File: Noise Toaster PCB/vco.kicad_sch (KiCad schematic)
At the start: 18 parts, among them Q3 2N3904, Q4 2N3904, U1 LM324

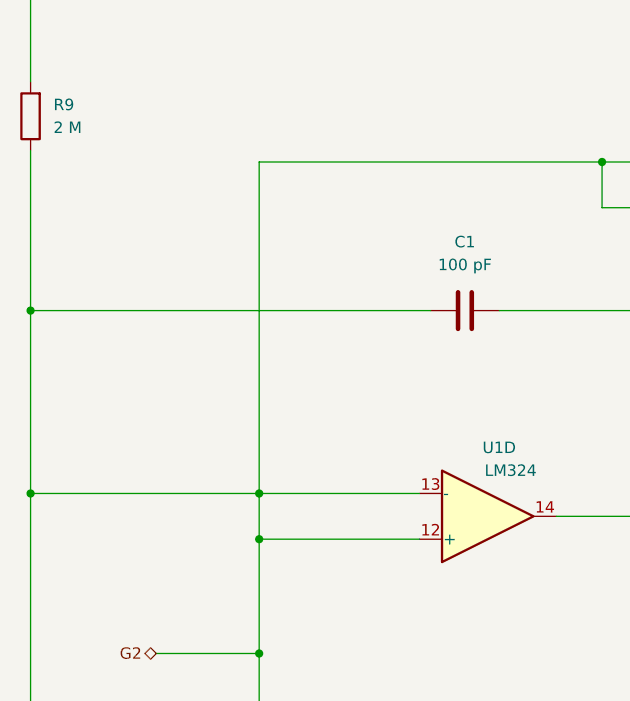
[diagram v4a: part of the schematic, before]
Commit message: placed pards of the pcb properly
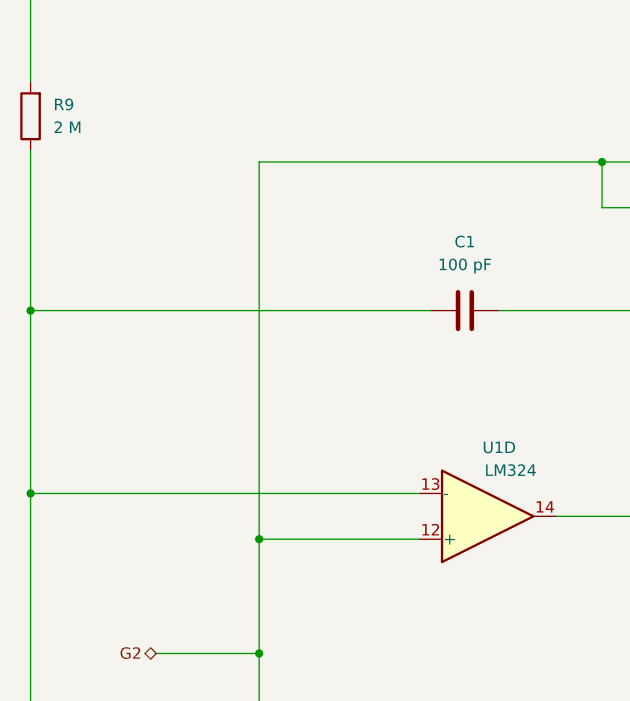
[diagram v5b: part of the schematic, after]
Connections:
- net G2: no longer C1.1, Q3.3 (C), R9.1, U1.13 (-)
- new net: C1.1, Q3.3 (C), R9.1, U1.13 (-)
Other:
- company: http://musicfromouterspace.com/analogsynth_new/NOISETOASTER/NOISETOASTER.php -> Music From Outer Space LLC
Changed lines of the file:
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@@
     (title "VCO - CV Mixer and Expo Converter")
     (rev "0.5")
-    (company "http://musicfromouterspace.com/analogsynth_new/NOISETOASTER/NOISETOASTER.php")
+    (company "Music From Outer Space LLC")
     (comment 1 "Licence: CC-BY-NC-SA")
     (comment 2 "Original Design by Ray Wilson")
-    (comment 3 "Music From Outer Space LLC")
+    (comment 3 "http://musicfromouterspace.com/analogsynth_new/NOISETOASTER/NOISETOASTER.php")
   )
   (junction (at 114.3 63.5) (diameter 0) (color 0 0 0 0)
@@
   (junction (at 88.9 110.49) (diameter 0) (color 0 0 0 0)
   )
-  (junction (at 50.8 147.32) (diameter 0) (color 0 0 0 0)
-  )
   (junction (at 25.4 147.32) (diameter 0) (color 0 0 0 0)
   )
@@
     (stroke (width 0) (type default))
   )
-  (wire (pts (xy 50.8 110.49) (xy 50.8 147.32))
+  (wire (pts (xy 50.8 110.49) (xy 50.8 152.4))
     (stroke (width 0) (type default))
   )
@@
     (stroke (width 0) (type default))
   )
-  (wire (pts (xy 50.8 152.4) (xy 50.8 147.32))
-    (stroke (width 0) (type default))
-  )
   (wire (pts (xy 88.9 110.49) (xy 88.9 115.57))
     (stroke (width 0) (type default))
@@
     (stroke (width 0) (type default))
   )
-  (wire (pts (xy 68.58 147.32) (xy 50.8 147.32))
-    (stroke (width 0) (type default))
-  )
   (wire (pts (xy 129.54 107.95) (xy 152.4 107.95))
     (stroke (width 0) (type default))
@@
     (stroke (width 0) (type default))
   )
-  (wire (pts (xy 50.8 147.32) (xy 25.4 147.32))
-    (stroke (width 0) (type default))
-  )
+  (wire (pts (xy 25.4 147.32) (xy 68.58 147.32))
+    (stroke (width 0) (type default))
+  )

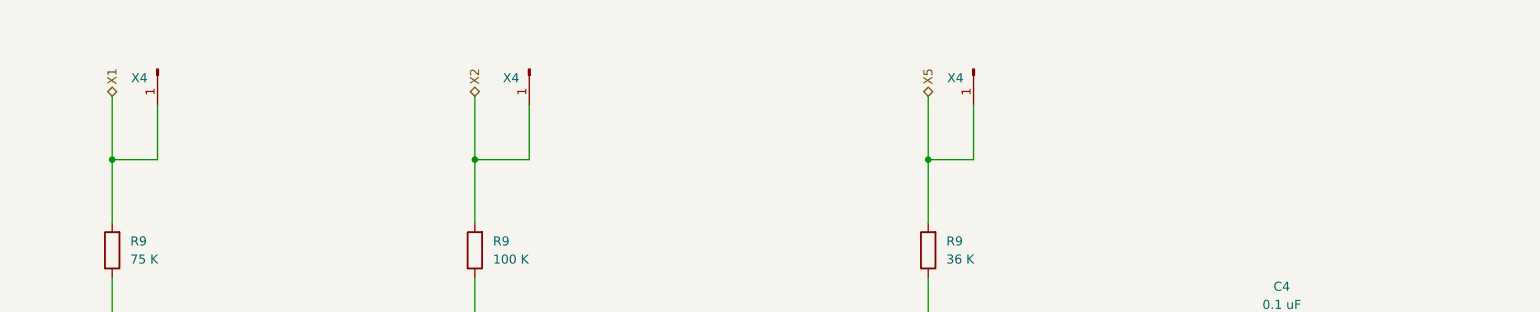
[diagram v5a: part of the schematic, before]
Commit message: changed header pins to groups
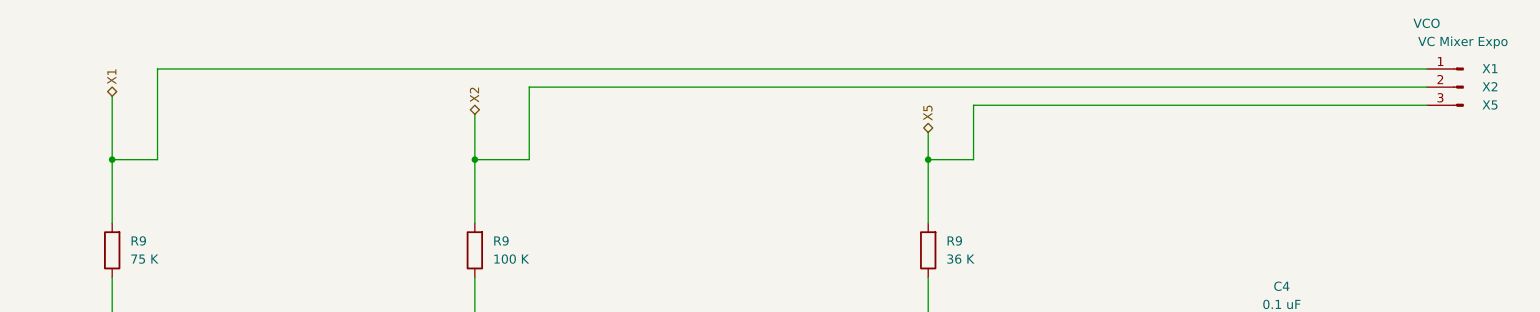
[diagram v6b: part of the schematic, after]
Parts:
- removed X4 (x3): ~, Connector_PinHeader_1.00mm:PinHeader_1x01_P1.00mm_Vertical, symbol Connector:Conn_01x01_Pin
- added J5: VCO, Connector_PinHeader_2.00mm:PinHeader_1x03_P2.00mm_Vertical, symbol Connector:Conn_01x03_Pin
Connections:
- net X1: now also J5.1 (Pin_1)
- net X2: now also J5.2 (Pin_2)
- net X5: now also J5.3 (Pin_3)
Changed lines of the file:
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@@
   (title_block
     (title "VCO - CV Mixer and Expo Converter")
-    (rev "0.5")
+    (rev "0.6")
     (company "Music From Outer Space LLC")
     (comment 1 "Licence: CC-BY-NC-SA")
@@
   (junction (at 101.6 127) (diameter 0) (color 0 0 0 0)
   )
+  (junction (at 114.3 83.82) (diameter 0) (color 0 0 0 0)
+  )
+  (junction (at 25.4 127) (diameter 0) (color 0 0 0 0)
+  )
   (junction (at 114.3 38.1) (diameter 0) (color 0 0 0 0)
   )
-  (junction (at 114.3 83.82) (diameter 0) (color 0 0 0 0)
-  )
-  (junction (at 25.4 127) (diameter 0) (color 0 0 0 0)
-  )
   (junction (at 25.4 83.82) (diameter 0) (color 0 0 0 0)
   )
   (junction (at 212.09 115.57) (diameter 0) (color 0 0 0 0)
   )
+  (junction (at 63.5 38.1) (diameter 0) (color 0 0 0 0)
+  )
   (junction (at 50.8 152.4) (diameter 0) (color 0 0 0 0)
   )
@@
   (junction (at 50.8 165.1) (diameter 0) (color 0 0 0 0)
   )
-  (junction (at 63.5 38.1) (diameter 0) (color 0 0 0 0)
-  )
   (junction (at 152.4 107.95) (diameter 0) (color 0 0 0 0)
   )
@@
     (stroke (width 0) (type default))
   )
+  (wire (pts (xy 247.65 25.4) (xy 69.85 25.4))
+    (stroke (width 0) (type default))
+  )
   (wire (pts (xy 114.3 38.1) (xy 121.92 38.1))
     (stroke (width 0) (type default))
@@
     (stroke (width 0) (type default))
   )
+  (wire (pts (xy 63.5 29.21) (xy 63.5 38.1))
+    (stroke (width 0) (type default))
+  )
+  (wire (pts (xy 137.16 83.82) (xy 152.4 83.82))
+    (stroke (width 0) (type default))
+  )
+  (wire (pts (xy 101.6 127) (xy 101.6 149.86))
+    (stroke (width 0) (type default))
+  )
+  (wire (pts (xy 114.3 63.5) (xy 114.3 83.82))
+    (stroke (width 0) (type default))
+  )
+  (wire (pts (xy 223.52 63.5) (xy 212.09 63.5))
+    (stroke (width 0) (type default))
+  )
+  (wire (pts (xy 88.9 110.49) (xy 88.9 115.57))
+    (stroke (width 0) (type default))
+  )
+  (wire (pts (xy 69.85 25.4) (xy 69.85 38.1))
+    (stroke (width 0) (type default))
+  )
+  (wire (pts (xy 243.84 152.4) (xy 255.27 152.4))
+    (stroke (width 0) (type default))
+  )
+  (wire (pts (xy 184.15 30.48) (xy 247.65 30.48))
+    (stroke (width 0) (type default))
+  )
+  (wire (pts (xy 114.3 54.61) (xy 114.3 63.5))
+    (stroke (width 0) (type default))
+  )
+  (wire (pts (xy 25.4 30.48) (xy 25.4 83.82))
+    (stroke (width 0) (type default))
+  )
+  (wire (pts (xy 177.8 38.1) (xy 177.8 46.99))
+    (stroke (width 0) (type default))
+  )
   (wire (pts (xy 63.5 38.1) (xy 63.5 46.99))
     (stroke (width 0) (type default))
   )
-  (wire (pts (xy 137.16 83.82) (xy 152.4 83.82))
-    (stroke (width 0) (type default))
-  )
-  (wire (pts (xy 101.6 127) (xy 101.6 149.86))
-    (stroke (width 0) (type default))
-  )
-  (wire (pts (xy 114.3 63.5) (xy 114.3 83.82))
-    (stroke (width 0) (type default))
-  )
-  (wire (pts (xy 223.52 63.5) (xy 212.09 63.5))
-    (stroke (width 0) (type default))
-  )
-  (wire (pts (xy 88.9 110.49) (xy 88.9 115.57))
-    (stroke (width 0) (type default))
-  )
-  (wire (pts (xy 69.85 30.48) (xy 69.85 38.1))
-    (stroke (width 0) (type default))
-  )
-  (wire (pts (xy 243.84 152.4) (xy 255.27 152.4))
-    (stroke (width 0) (type default))
-  )
-  (wire (pts (xy 114.3 54.61) (xy 114.3 63.5))
-    (stroke (width 0) (type default))
-  )
-  (wire (pts (xy 25.4 30.48) (xy 25.4 83.82))
-    (stroke (width 0) (type default))
-  )
-  (wire (pts (xy 177.8 29.21) (xy 177.8 38.1))
-    (stroke (width 0) (type default))
-  )
   (wire (pts (xy 232.41 88.9) (xy 243.84 88.9))
     (stroke (width 0) (type default))
@@
     (stroke (width 0) (type default))
   )
-  (wire (pts (xy 63.5 29.21) (xy 63.5 38.1))
-    (stroke (width 0) (type default))
-  )
   (wire (pts (xy 212.09 88.9) (xy 212.09 115.57))
     (stroke (width 0) (type default))
@@
     (stroke (width 0) (type default))
   )
+  (wire (pts (xy 114.3 38.1) (xy 114.3 46.99))
+    (stroke (width 0) (type default))
+  )
+  (wire (pts (xy 247.65 27.94) (xy 121.92 27.94))
+    (stroke (width 0) (type default))
+  )
   (wire (pts (xy 129.54 107.95) (xy 152.4 107.95))
     (stroke (width 0) (type default))
@@
     (stroke (width 0) (type default))
   )
-  (wire (pts (xy 121.92 30.48) (xy 121.92 38.1))
-    (stroke (width 0) (type default))
-  )
-  (wire (pts (xy 177.8 38.1) (xy 177.8 46.99))
+  (wire (pts (xy 121.92 27.94) (xy 121.92 38.1))
+    (stroke (width 0) (type default))
+  )
+  (wire (pts (xy 177.8 34.29) (xy 177.8 38.1))
     (stroke (width 0) (type default))
   )
@@
     (stroke (width 0) (type default))
   )
-  (wire (pts (xy 114.3 29.21) (xy 114.3 38.1))
-    (stroke (width 0) (type default))
-  )
   (wire (pts (xy 212.09 133.35) (xy 224.79 133.35))
     (stroke (width 0) (type default))
@@
     (stroke (width 0) (type default))
   )
-  (wire (pts (xy 114.3 38.1) (xy 114.3 46.99))
+  (wire (pts (xy 114.3 31.75) (xy 114.3 38.1))
     (stroke (width 0) (type default))
   )
@@
     (effects (font (size 1.27 1.27)) (justify left))
   )
-  (hierarchical_label "X2" (shape bidirectional) (at 114.3 29.21 90) (fields_autoplaced)
+  (hierarchical_label "X2" (shape bidirectional) (at 114.3 31.75 90) (fields_autoplaced)
     (effects (font (size 1.27 1.27)) (justify left))
   )
@@
     (effects (font (size 1.27 1.27)) (justify right))
   )
-  (hierarchical_label "X5" (shape bidirectional) (at 177.8 29.21 90) (fields_autoplaced)
+  (hierarchical_label "X5" (shape bidirectional) (at 177.8 34.29 90) (fields_autoplaced)
     (effects (font (size 1.27 1.27)) (justify left))
   )
@@
     )
   )
-  (symbol (lib_id "Connector:Conn_01x01_Pin") (at 121.92 25.4 270) (unit 1)
-    (in_bom yes) (on_board yes) (dnp no)
-    (property "Reference" "X4" (at 119.38 26.67 90)
-      (effects (font (size 1.27 1.27)))
-    )
-    (property "Value" "~" (at 124.46 26.035 0)
-      (effects (font (size 1.27 1.27)))
-    )
-    (property "Footprint" "Connector_PinHeader_1.00mm:PinHeader_1x01_P1.00mm_Vertical" (at 121.92 25.4 0)
-      (effects (font (size 1.27 1.27)) hide)
-    )
-    (property "Datasheet" "~" (at 121.92 25.4 0)
-      (effects (font (size 1.27 1.27)) hide)
-    )
-    (pin "1")
-    (instances
-      (project "Noise Toaster PCB"
-        (path "/7be3f398-d902-4566-9ee4-0bff072cd47e/818b46cb-815d-4132-b52d-9731333b7f1f"
-          (reference "X4") (unit 1)
-        )
-        (path "/7be3f398-d902-4566-9ee4-0bff072cd47e/d0369b76-3398-4137-86ba-22490a5aca99"
-          (reference "X2") (unit 1)
+  (symbol (lib_id "Connector:Conn_01x03_Pin") (at 252.73 27.94 0) (mirror y) (unit 1)
+    (in_bom yes) (on_board yes) (dnp no)
+    (property "Reference" "J5" (at 252.095 20.32 0)
+      (effects (font (size 1.27 1.27)) hide)
+    )
+    (property "Value" "VCO" (at 247.65 19.05 0)
+      (effects (font (size 1.27 1.27)))
+    )
+    (property "Footprint" "Connector_PinHeader_2.00mm:PinHeader_1x03_P2.00mm_Vertical" (at 252.73 27.94 0)
+      (effects (font (size 1.27 1.27)) hide)
+    )
+    (property "Datasheet" "~" (at 252.73 27.94 0)
+      (effects (font (size 1.27 1.27)) hide)
+    )
+    (property "Wert2" "VC Mixer Expo" (at 252.73 21.59 0)
+      (effects (font (size 1.27 1.27)))
+    )
+    (property "X1" "X1" (at 256.54 25.4 0)
+      (effects (font (size 1.27 1.27)))
+    )
+    (property "X2" "X2" (at 256.54 27.94 0)
+      (effects (font (size 1.27 1.27)))
+    )
+    (property "X5" "X5" (at 256.54 30.48 0)
+      (effects (font (size 1.27 1.27)))
+    )
+    (pin "1")
+    (pin "2")
+    (pin "3")
+    (instances
+      (project "Noise Toaster PCB"
+        (path "/7be3f398-d902-4566-9ee4-0bff072cd47e/d0369b76-3398-4137-86ba-22490a5aca99"
+          (reference "J5") (unit 1)
         )
       )
@@
     )
   )
-  (symbol (lib_id "Connector:Conn_01x01_Pin") (at 69.85 25.4 270) (unit 1)
-    (in_bom yes) (on_board yes) (dnp no)
-    (property "Reference" "X4" (at 67.31 26.67 90)
-      (effects (font (size 1.27 1.27)))
-    )
-    (property "Value" "~" (at 72.39 26.035 0)
-      (effects (font (size 1.27 1.27)))
-    )
-    (property "Footprint" "Connector_PinHeader_1.00mm:PinHeader_1x01_P1.00mm_Vertical" (at 69.85 25.4 0)
-      (effects (font (size 1.27 1.27)) hide)
-    )
-    (property "Datasheet" "~" (at 69.85 25.4 0)
-      (effects (font (size 1.27 1.27)) hide)
-    )
-    (pin "1")
-    (instances
-      (project "Noise Toaster PCB"
-        (path "/7be3f398-d902-4566-9ee4-0bff072cd47e/818b46cb-815d-4132-b52d-9731333b7f1f"
-          (reference "X4") (unit 1)
-        )
-        (path "/7be3f398-d902-4566-9ee4-0bff072cd47e/d0369b76-3398-4137-86ba-22490a5aca99"
-          (reference "X1") (unit 1)
-        )
-      )
-    )
-  )
   (symbol (lib_id "Transistor_BJT:2N3904") (at 114.3 173.99 0) (mirror x) (unit 1)
     (in_bom yes) (on_board yes) (dnp no)
@@
         )
       )
-    )
-  )
-  (symbol (lib_id "Connector:Conn_01x01_Pin") (at 184.15 25.4 270) (unit 1)
-    (in_bom yes) (on_board yes) (dnp no)
-    (property "Reference" "X4" (at 181.61 26.67 90)
-      (effects (font (size 1.27 1.27)))
-    )
-    (property "Value" "~" (at 186.69 26.035 0)
-      (effects (font (size 1.27 1.27)))
-    )
-    (property "Footprint" "Connector_PinHeader_1.00mm:PinHeader_1x01_P1.00mm_Vertical" (at 184.15 25.4 0)
-      (effects (font (size 1.27 1.27)) hide)
-    )
-    (property "Datasheet" "~" (at 184.15 25.4 0)
-      (effects (font (size 1.27 1.27)) hide)
-    )
-    (pin "1")
-    (instances
-      (project "Noise Toaster PCB"
-        (path "/7be3f398-d902-4566-9ee4-0bff072cd47e/818b46cb-815d-4132-b52d-9731333b7f1f"
-          (reference "X4") (unit 1)
-        )
-        (path "/7be3f398-d902-4566-9ee4-0bff072cd47e/d0369b76-3398-4137-86ba-22490a5aca99"
-          (reference "X5") (unit 1)
-        )
-      )
